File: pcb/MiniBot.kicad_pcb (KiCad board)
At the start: 4 copper layers, 21.2 x 28 mm, 60 parts, among them IC1 MMC5633NJL, IC2 MIC23050-SYML-TR, J1 Conn_01x08, J2 Conn_01x02, J3 GSB1C41110SSHR, J4 Conn_01x01, U1 ESP32-C3-MINI-1-H4X, U3 MCP73832-2-OT, U4 STSPIN220, U5 STSPIN220

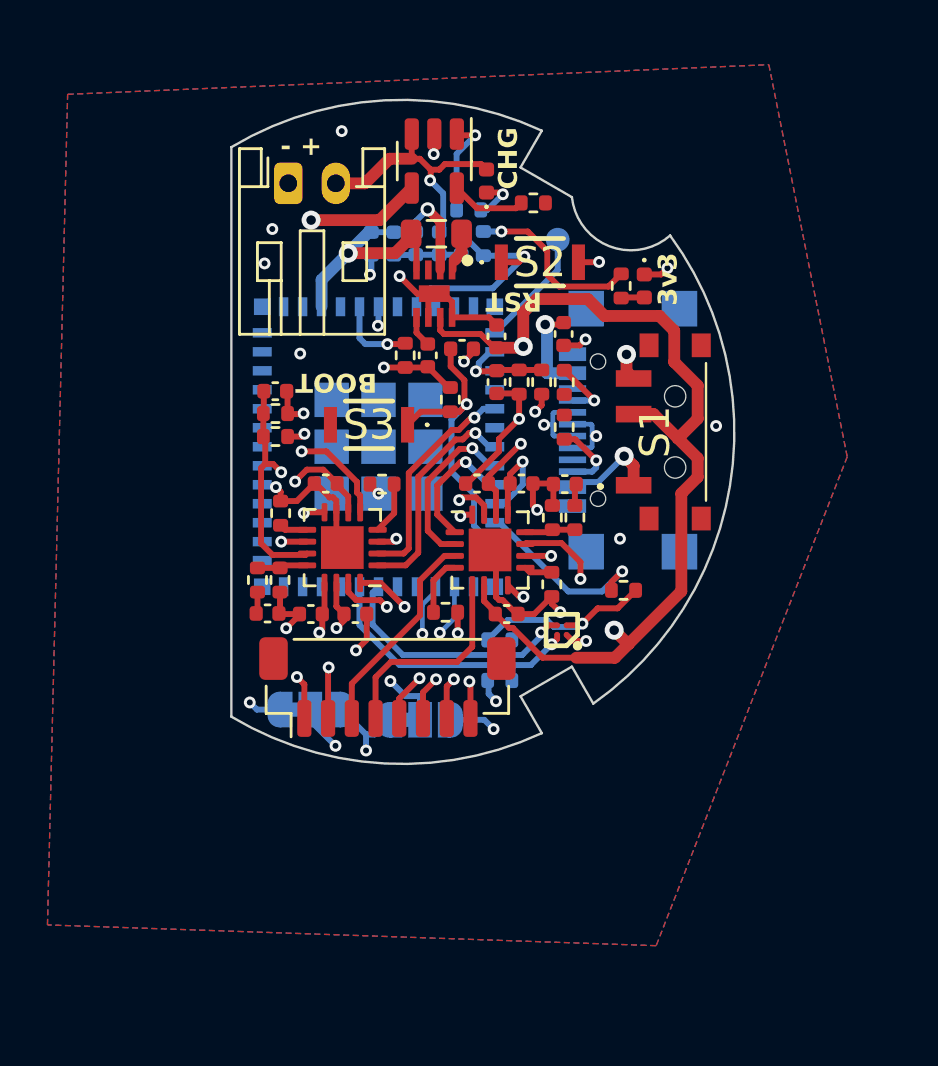
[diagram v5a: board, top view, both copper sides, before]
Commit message: reorg and write device ID to NVS
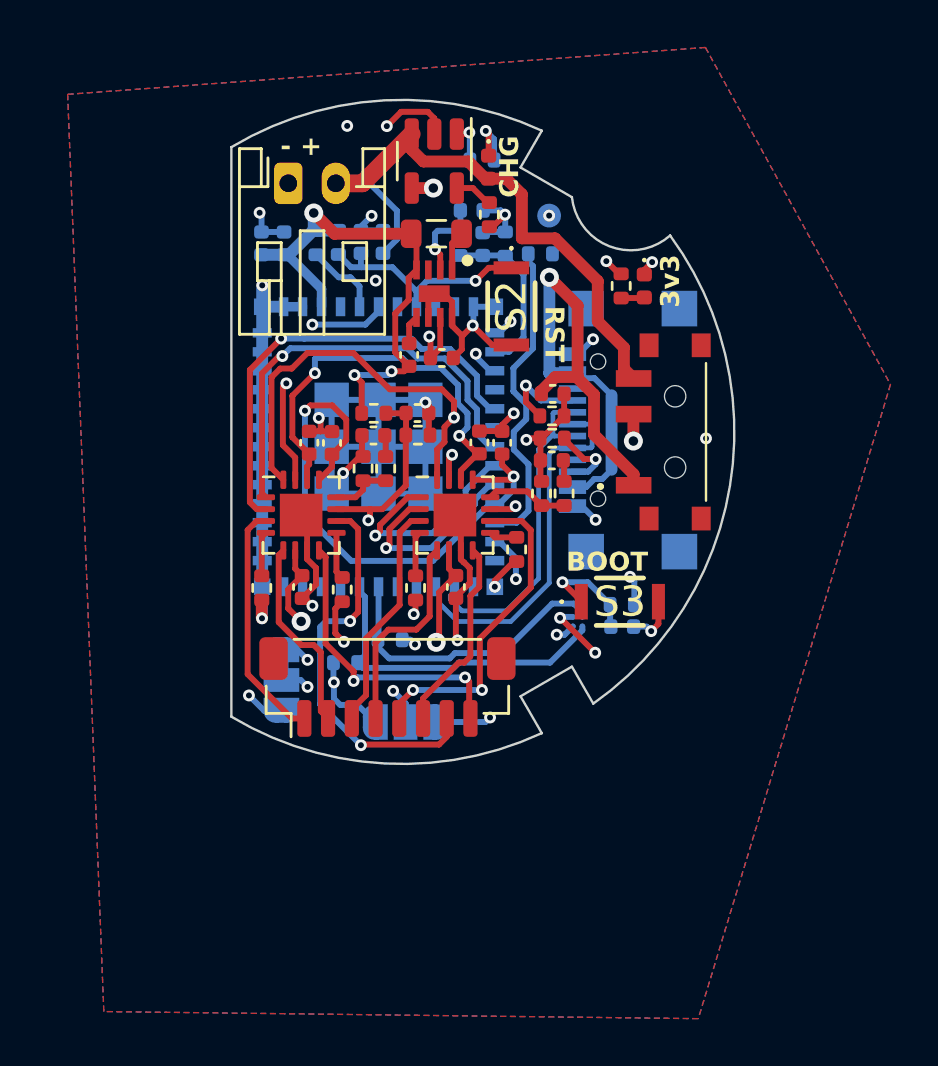
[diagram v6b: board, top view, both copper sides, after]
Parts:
- C5, C6, IC1, R10, R11, R5, R6, R9: moved to B.Cu
- moved R5 14.6 mm to (127.2, 91.4)
- moved C5 13.5 mm to (130.6, 107.1)
- moved S3 12.9 mm to (130.5, 106.1), turned to 0 degrees
- moved R9 11.3 mm to (130.6, 106.2), turned to 180 degrees
- moved C18 8.73 mm to (120.1, 99.1), turned to 180 degrees
- moved C16 7.48 mm to (117.4, 99.4), turned to 90 degrees
- moved C15 7.26 mm to (118.4, 99.4), turned to 90 degrees
- moved R16 7.16 mm to (120.7, 100.5), turned to 90 degrees
- moved R10 6.78 mm to (123.8, 91.0), turned to -90 degrees
- moved R19 6.70 mm to (115.4, 105.5), turned to -90 degrees
- moved R1 6.54 mm to (119.0, 108.7)
- moved R3 6.11 mm to (118.7, 90.9)
- moved JP2 6.08 mm to (116.3, 109.4), turned to -90 degrees
- moved R8 6.07 mm to (122.0, 99.1)
- moved C4 6.06 mm to (122.0, 98.1)
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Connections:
- JP1 pad 1: +3V3 -> GND
- JP1 pad 3: GND -> +3V3
- JP2 pad 1: GND -> +3V3
- JP2 pad 3: +3V3 -> GND
- U1 pad 19: /M1_STEP -> /M1_DIR
- U1 pad 20: /M1_DIR -> /M1_STEP
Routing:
- net GND: track 48.6 -> 96.6 mm, vias 22 -> 25
- net VDC: track 76.4 -> 49.3 mm
- net /MODE1: track 14.5 -> 35.9 mm, vias 3 -> 2
- net /MODE2: track 19.0 -> 36.5 mm
- net /VREF: track 28.8 -> 15.3 mm
- net /M0_A2: track 18.4 -> 8.33 mm, vias 2 -> 0
- net /M0_STEP: track 9.33 -> 19.0 mm
- net /M0_DIR: track 9.36 -> 18.3 mm
- net /M_RST: track 29.1 -> 22.7 mm
- net /GPIO8: track 7.91 -> 13.6 mm, vias 1 -> 0
- net +3V3: track 43.7 -> 38.2 mm, vias 10 -> 13
- net +BATT: track 29.9 -> 25.8 mm, vias 2 -> 0
- net /M0_B1: track 12.6 -> 16.7 mm
- net /GPIO9: track 12.4 -> 8.57 mm, vias 1 -> 2
- net /M1_DIR: track 5.70 -> 9.18 mm
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- added copper zone on B.Cu, net +3V3
- added copper zone on F.Cu, net +3V3
- added copper zone on In1.Cu, net GND
- added copper zone on In2.Cu, net VDC
- removed copper zone on In1.Cu, net +3V3
- removed copper zone on In2.Cu, net +3V3
- removed copper zone on B.Cu, net GND
- removed copper zone on F.Cu, net GND
